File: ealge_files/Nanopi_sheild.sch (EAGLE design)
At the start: 2 parts, among them U1 52207-0885

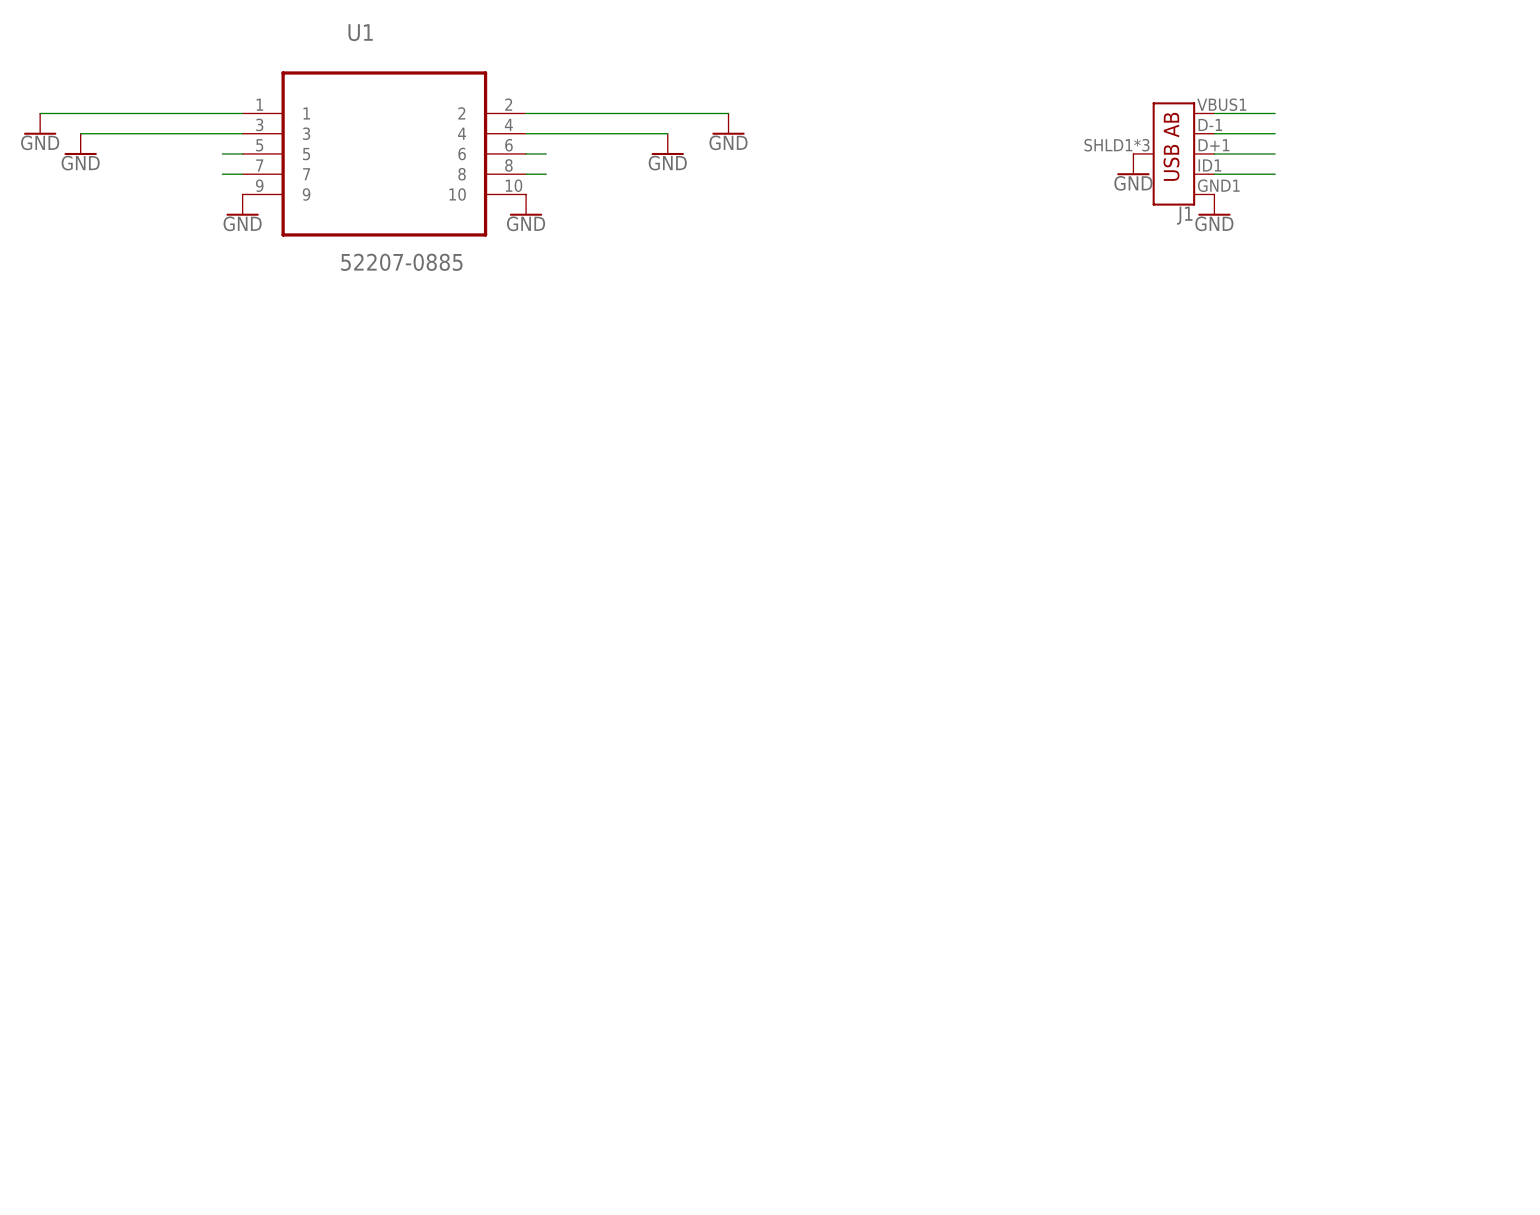
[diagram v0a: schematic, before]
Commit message: added few libraries and completed all schematic
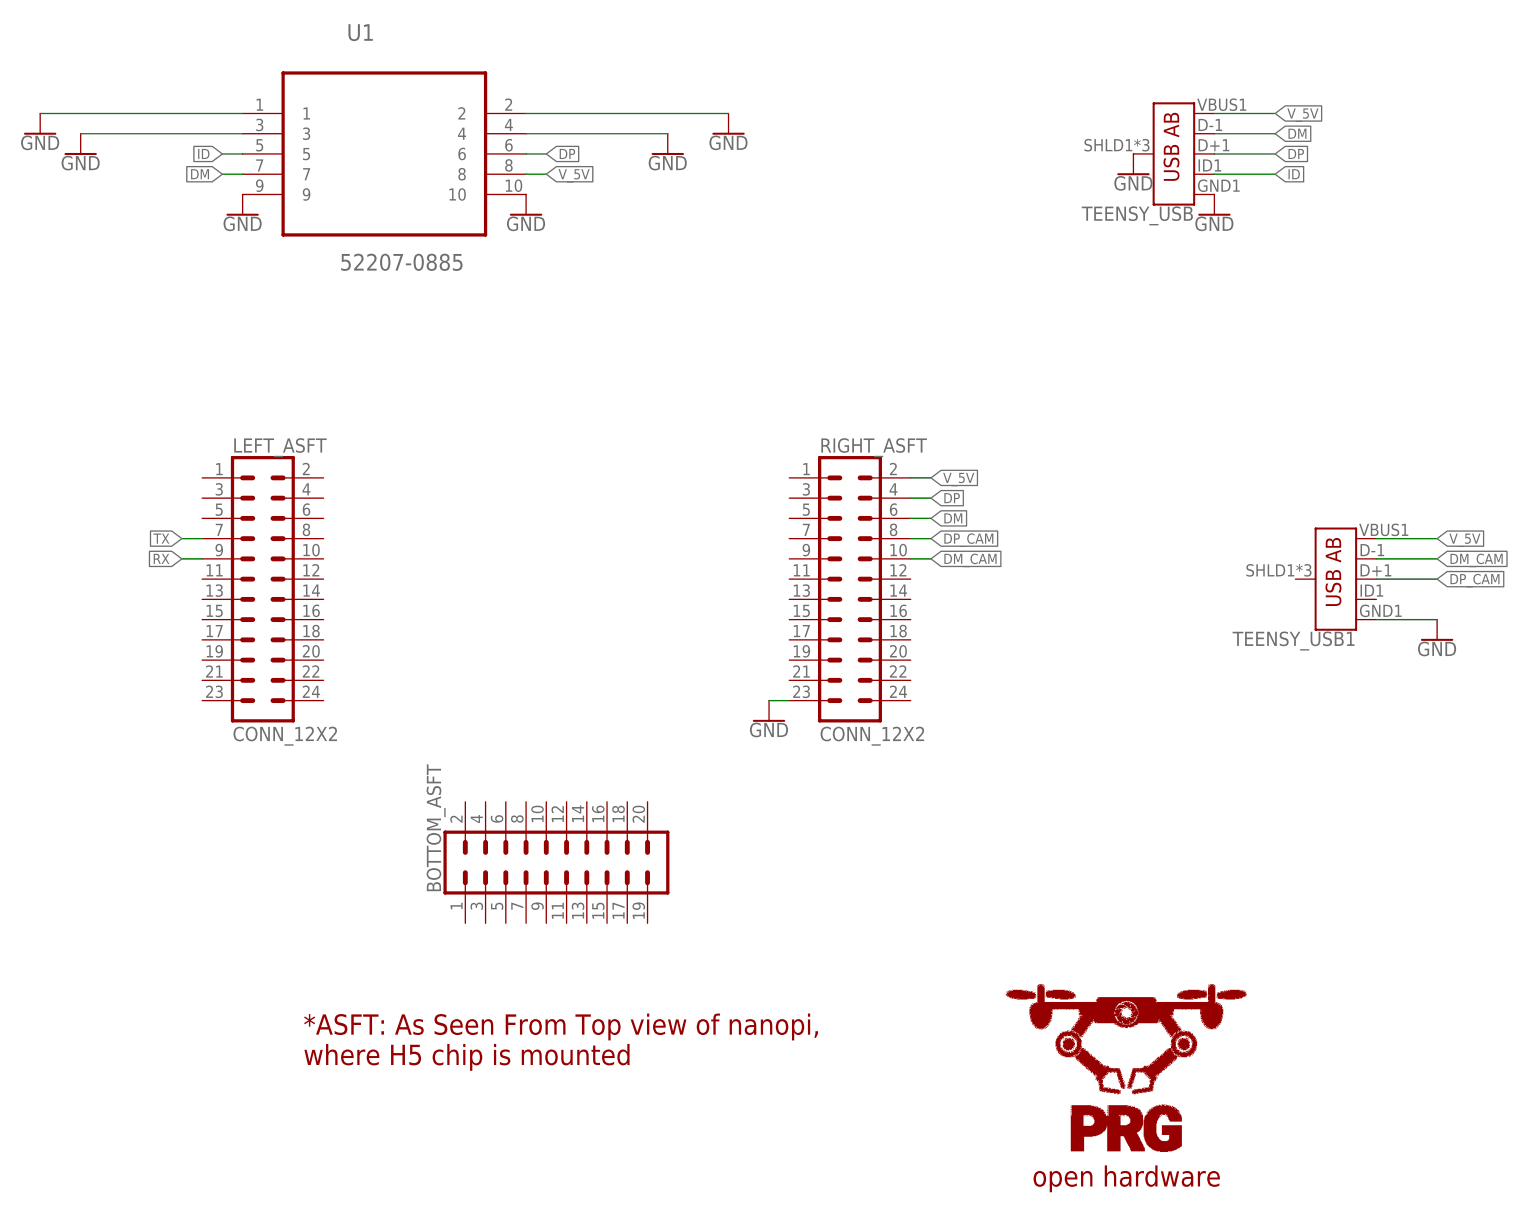
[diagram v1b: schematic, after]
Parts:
- added BOTTOM_ASFT: (no value), SparkFun-Connectors:CONN_10X2
- added LEFT_ASFT, RIGHT_ASFT: CONN_12X2, SparkFun-Connectors:CONN_12X2
- added TEENSY_USB1: (no value), SparkFun-Connectors:USB_AB_SMT
- renumbered J1 to TEENSY_USB
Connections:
- removed net N$1: U1.5
- removed net N$2: U1.7
- removed net N$3: U1.6
- removed net N$4: U1.8
- removed net N$5: TEENSY_USB.VBUS
- removed net N$6: TEENSY_USB.D-
- removed net N$7: TEENSY_USB.D+
- removed net N$8: TEENSY_USB.USBID
- new net DM: RIGHT_ASFT.6, TEENSY_USB.D-, U1.7
- new net DM_CAM: RIGHT_ASFT.10, TEENSY_USB1.D-
- new net DP: RIGHT_ASFT.4, TEENSY_USB.D+, U1.6
- new net DP_CAM: RIGHT_ASFT.8, TEENSY_USB1.D+
- new net ID: TEENSY_USB.USBID, U1.5
- new net RX: LEFT_ASFT.9
- new net TX: LEFT_ASFT.7
- new net V_5V: RIGHT_ASFT.2, TEENSY_USB.VBUS, TEENSY_USB1.VBUS, U1.8
- net GND: now also RIGHT_ASFT.23, TEENSY_USB1.GND
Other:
- note added: "*ASFT: As Seen From Top view of nanopi, where H5 chip is mounted"
- note added: "open hardware"

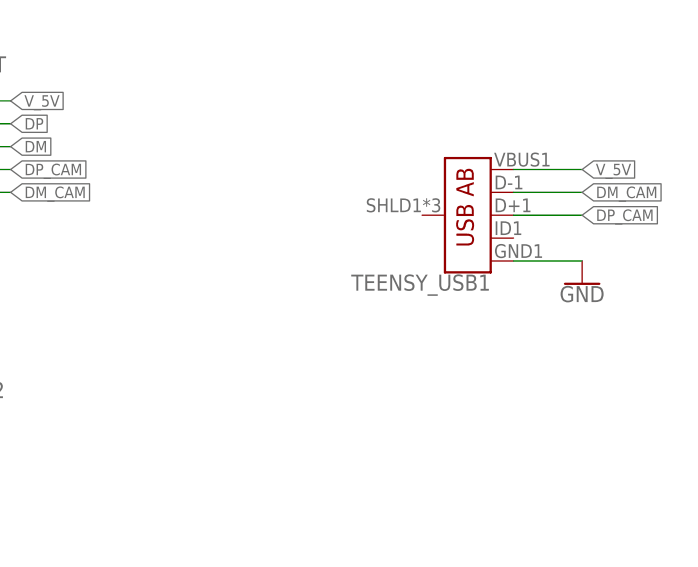
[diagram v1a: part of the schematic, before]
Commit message: updated nanopi shield
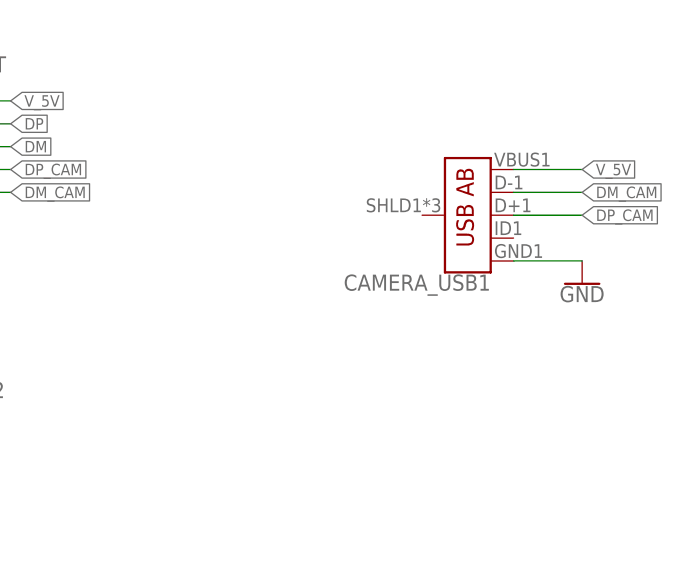
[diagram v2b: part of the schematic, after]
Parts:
- renumbered TEENSY_USB1 to CAMERA_USB1
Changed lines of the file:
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@@
 <part name="BOTTOM_ASFT" library="SparkFun-Connectors" library_urn="urn:adsk.eagle:library:513" deviceset="CONN_10X2" device="" package3d_urn="urn:adsk.eagle:package:38291/1"/>
 <part name="GND9" library="SparkFun-PowerSymbols" library_urn="urn:adsk.eagle:library:530" deviceset="GND" device=""/>
-<part name="TEENSY_USB1" library="SparkFun-Connectors" library_urn="urn:adsk.eagle:library:513" deviceset="USB_AB" device="_SMT" package3d_urn="urn:adsk.eagle:package:38266/1"/>
+<part name="CAMERA_USB1" library="SparkFun-Connectors" library_urn="urn:adsk.eagle:library:513" deviceset="USB_AB" device="_SMT" package3d_urn="urn:adsk.eagle:package:38266/1"/>
 <part name="GND10" library="SparkFun-PowerSymbols" library_urn="urn:adsk.eagle:library:530" deviceset="GND" device=""/>
 </parts>
@@
 <attribute name="VALUE" x="96.52" y="-2.794" size="1.778" layer="96" align="top-center"/>
 </instance>
-<instance part="TEENSY_USB1" gate="G$1" x="167.64" y="15.24" smashed="yes" rot="R180">
+<instance part="CAMERA_USB1" gate="G$1" x="167.64" y="15.24" smashed="yes" rot="R180">
 <attribute name="NAME" x="170.18" y="8.636" size="1.778" layer="95" font="vector" rot="R180"/>
 <attribute name="VALUE" x="170.18" y="21.844" size="1.778" layer="96" font="vector" rot="R180" align="top-left"/>
@@
 </segment>
 <segment>
-<pinref part="TEENSY_USB1" gate="G$1" pin="GND"/>
+<pinref part="CAMERA_USB1" gate="G$1" pin="GND"/>
 <wire x1="172.72" y1="10.16" x2="180.34" y2="10.16" width="0.1524" layer="91"/>
 <pinref part="GND10" gate="1" pin="GND"/>
@@
 </segment>
 <segment>
-<pinref part="TEENSY_USB1" gate="G$1" pin="VBUS"/>
+<pinref part="CAMERA_USB1" gate="G$1" pin="VBUS"/>
 <wire x1="172.72" y1="20.32" x2="180.34" y2="20.32" width="0.1524" layer="91"/>
 <label x="180.34" y="20.32" size="1.27" layer="95" xref="yes"/>
@@
 <net name="DM_CAM" class="0">
 <segment>
-<pinref part="TEENSY_USB1" gate="G$1" pin="D-"/>
+<pinref part="CAMERA_USB1" gate="G$1" pin="D-"/>
 <wire x1="172.72" y1="17.78" x2="180.34" y2="17.78" width="0.1524" layer="91"/>
 <label x="180.34" y="17.78" size="1.27" layer="95" xref="yes"/>
@@
 <net name="DP_CAM" class="0">
 <segment>
-<pinref part="TEENSY_USB1" gate="G$1" pin="D+"/>
+<pinref part="CAMERA_USB1" gate="G$1" pin="D+"/>
 <wire x1="172.72" y1="15.24" x2="180.34" y2="15.24" width="0.1524" layer="91"/>
 <label x="180.34" y="15.24" size="1.27" layer="95" xref="yes"/>

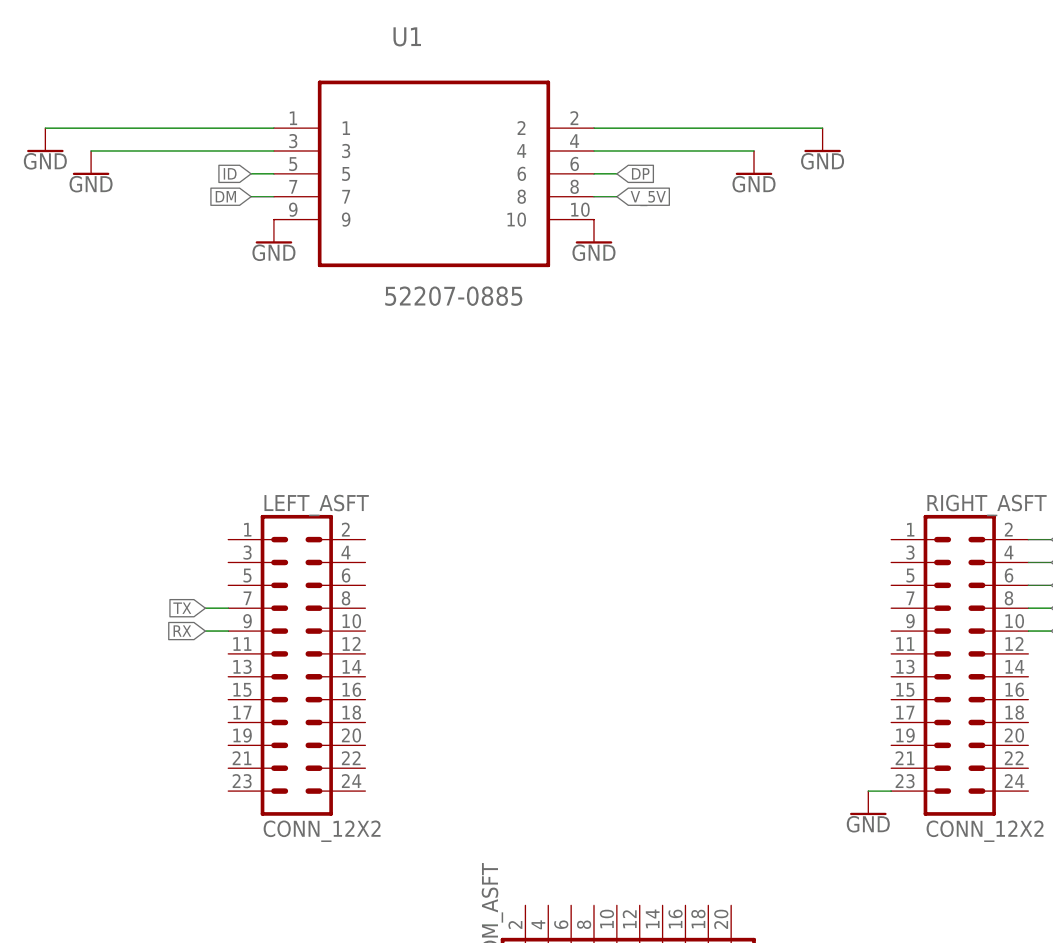
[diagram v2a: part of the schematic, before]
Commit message: added molex for cam
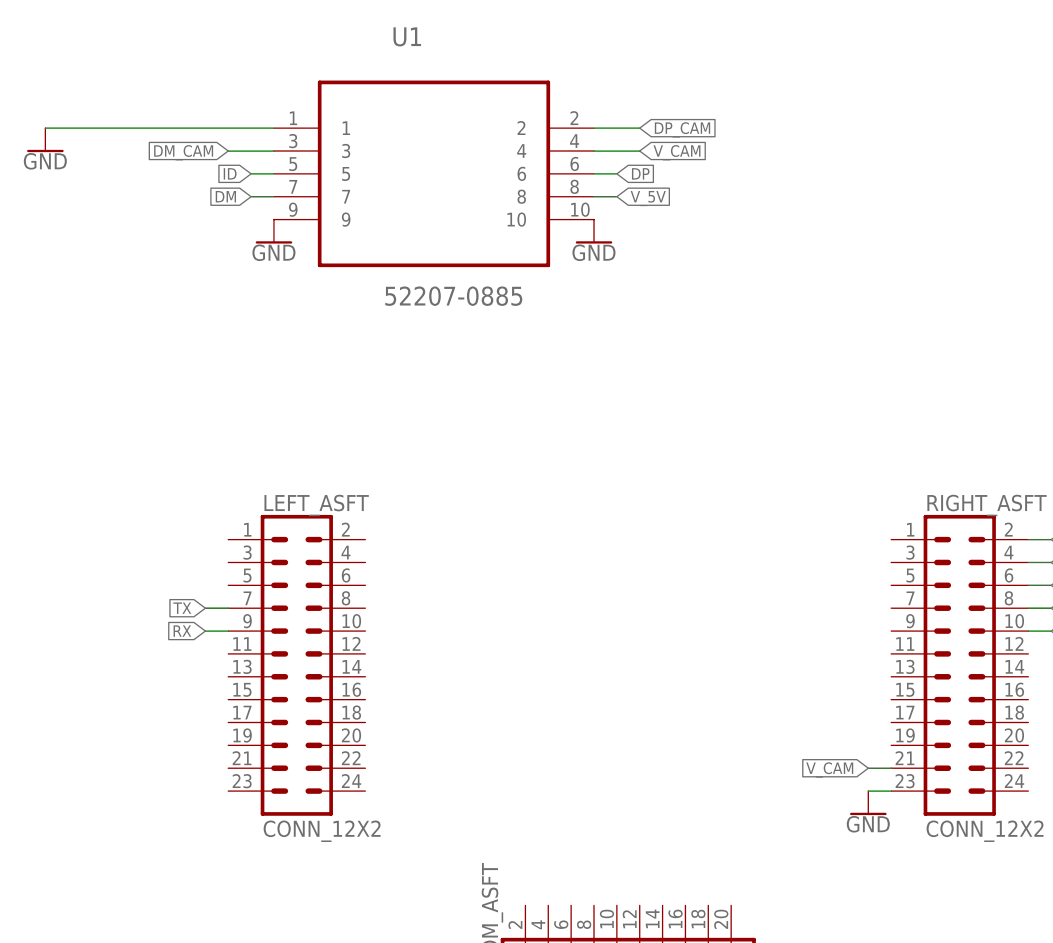
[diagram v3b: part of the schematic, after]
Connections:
- new net V_CAM: RIGHT_ASFT.21, U1.4
- net DM_CAM: now also U1.3
- net DP_CAM: now also U1.2
- net GND: no longer U1.2, U1.3, U1.4
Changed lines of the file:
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@@
 <part name="GND2" library="SparkFun-PowerSymbols" library_urn="urn:adsk.eagle:library:530" deviceset="GND" device=""/>
 <part name="GND3" library="SparkFun-PowerSymbols" library_urn="urn:adsk.eagle:library:530" deviceset="GND" device=""/>
-<part name="GND4" library="SparkFun-PowerSymbols" library_urn="urn:adsk.eagle:library:530" deviceset="GND" device=""/>
-<part name="GND5" library="SparkFun-PowerSymbols" library_urn="urn:adsk.eagle:library:530" deviceset="GND" device=""/>
-<part name="GND6" library="SparkFun-PowerSymbols" library_urn="urn:adsk.eagle:library:530" deviceset="GND" device=""/>
 <part name="GND7" library="SparkFun-PowerSymbols" library_urn="urn:adsk.eagle:library:530" deviceset="GND" device=""/>
 <part name="GND8" library="SparkFun-PowerSymbols" library_urn="urn:adsk.eagle:library:530" deviceset="GND" device=""/>
@@
 <attribute name="VALUE" x="5.08" y="70.866" size="1.778" layer="96" align="top-center"/>
 </instance>
-<instance part="GND4" gate="1" x="10.16" y="68.58" smashed="yes">
-<attribute name="VALUE" x="10.16" y="68.326" size="1.778" layer="96" align="top-center"/>
-</instance>
-<instance part="GND5" gate="1" x="83.82" y="68.58" smashed="yes">
-<attribute name="VALUE" x="83.82" y="68.326" size="1.778" layer="96" align="top-center"/>
-</instance>
-<instance part="GND6" gate="1" x="91.44" y="71.12" smashed="yes">
-<attribute name="VALUE" x="91.44" y="70.866" size="1.778" layer="96" align="top-center"/>
-</instance>
 <instance part="GND7" gate="1" x="142.24" y="66.04" smashed="yes">
 <attribute name="VALUE" x="142.24" y="65.786" size="1.778" layer="96" align="top-center"/>
@@
 </segment>
 <segment>
-<pinref part="GND4" gate="1" pin="GND"/>
-<pinref part="U1" gate="A" pin="3"/>
-<wire x1="10.16" y1="71.12" x2="30.48" y2="71.12" width="0.1524" layer="91"/>
-</segment>
-<segment>
-<pinref part="U1" gate="A" pin="2"/>
-<pinref part="GND6" gate="1" pin="GND"/>
-<wire x1="66.04" y1="73.66" x2="91.44" y2="73.66" width="0.1524" layer="91"/>
-</segment>
-<segment>
-<pinref part="GND5" gate="1" pin="GND"/>
-<wire x1="66.04" y1="71.12" x2="83.82" y2="71.12" width="0.1524" layer="91"/>
-<pinref part="U1" gate="A" pin="4"/>
-</segment>
-<segment>
 <pinref part="RIGHT_ASFT" gate="G$1" pin="23"/>
 <wire x1="99.06" y1="0" x2="96.52" y2="0" width="0.1524" layer="91"/>
@@
 <label x="116.84" y="17.78" size="1.27" layer="95" xref="yes"/>
 </segment>
+<segment>
+<pinref part="U1" gate="A" pin="3"/>
+<wire x1="30.48" y1="71.12" x2="25.4" y2="71.12" width="0.1524" layer="91"/>
+<label x="25.4" y="71.12" size="1.27" layer="95" rot="R180" xref="yes"/>
+</segment>
 </net>
 <net name="DP_CAM" class="0">
@@
 <label x="116.84" y="20.32" size="1.27" layer="95" xref="yes"/>
 </segment>
+<segment>
+<pinref part="U1" gate="A" pin="2"/>
+<wire x1="66.04" y1="73.66" x2="71.12" y2="73.66" width="0.1524" layer="91"/>
+<label x="71.12" y="73.66" size="1.27" layer="95" xref="yes"/>
+</segment>
 </net>
 <net name="TX" class="0">
@@
 </segment>
 </net>
+<net name="V_CAM" class="0">
+<segment>
+<pinref part="U1" gate="A" pin="4"/>
+<wire x1="66.04" y1="71.12" x2="71.12" y2="71.12" width="0.1524" layer="91"/>
+<label x="71.12" y="71.12" size="1.27" layer="95" xref="yes"/>
+</segment>
+<segment>
+<pinref part="RIGHT_ASFT" gate="G$1" pin="21"/>
+<wire x1="99.06" y1="2.54" x2="96.52" y2="2.54" width="0.1524" layer="91"/>
+<label x="96.52" y="2.54" size="1.27" layer="95" rot="R180" xref="yes"/>
+</segment>
+</net>
